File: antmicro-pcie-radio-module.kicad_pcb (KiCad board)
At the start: 4 copper layers, 80.2 x 22.2 mm, 54 parts, among them J1 U_FL-R-SMT_10_, J2 M.2-M+B-Pins, U1 UPD720202, U2 SST25VF512A, U3 CoralAccelerator, U4 NRF52840, U5 PE42423MLBA-Z, Y1 NX3225SA-24M

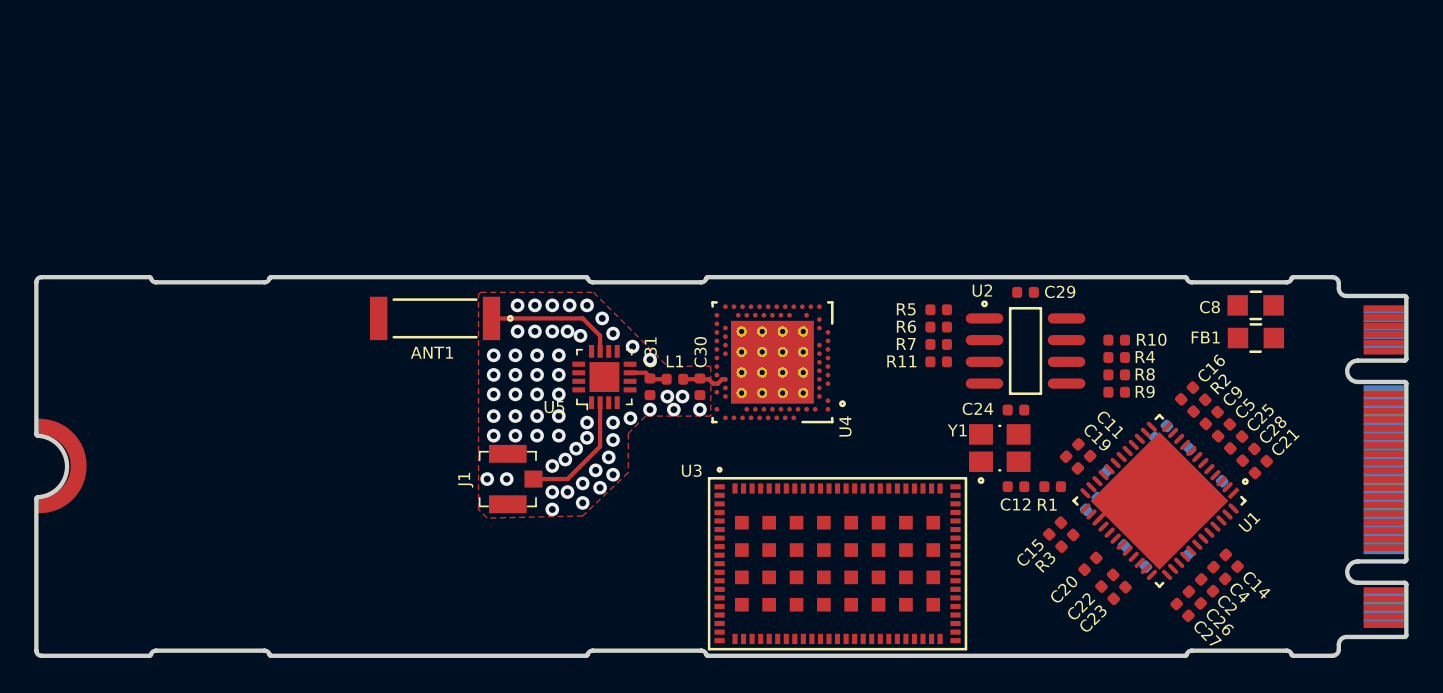
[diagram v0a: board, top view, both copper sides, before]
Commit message: Add initial component layout
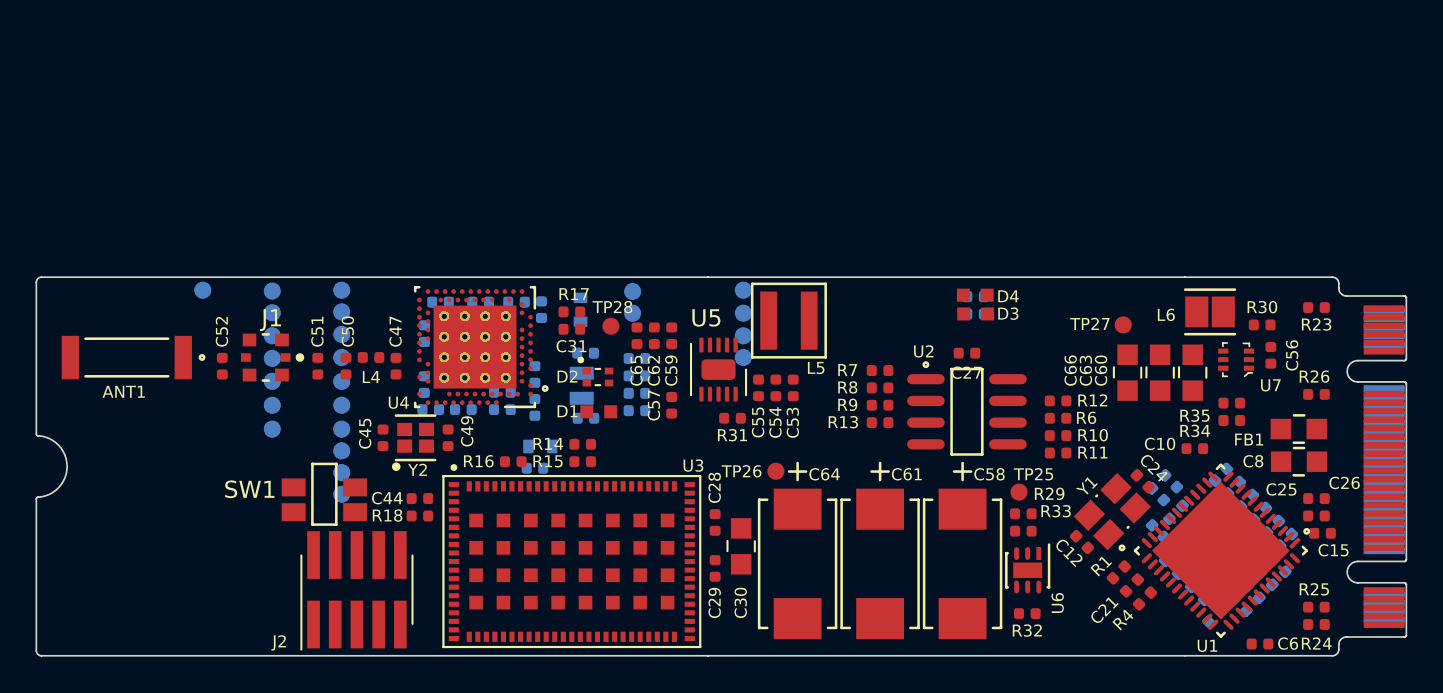
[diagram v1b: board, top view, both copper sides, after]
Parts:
- removed the C26 at (182.5, 110.2)
- removed the C27 at (181.8, 110.9)
- removed REF**: M.2 Stud, pcie-radio-module:M.2 Stud
- added C28: C_100n_0402, pcie-radio-module:0402-cap, F.Cu at (154.4, 105.8)
- added C29: C_100n_0402, pcie-radio-module:0402-cap, F.Cu at (154.4, 108.5)
- added C32: C_4u7_0402, pcie-radio-module:0402-cap, B.Cu at (142.8, 92.9)
- added C33: C_100n_0402, pcie-radio-module:0402-cap, B.Cu at (143.9, 97.1)
- added C34: C_100n_0402, pcie-radio-module:0402-cap, B.Cu at (139.7, 99.2)
- added C35: C_1u_0402, pcie-radio-module:0402-cap, B.Cu at (143.9, 99.1)
- added C36: C_100n_0402, pcie-radio-module:0402-cap, B.Cu at (140.7, 92.9)
- added C37: C_100p_0402, pcie-radio-module:0402-cap, B.Cu at (137.4, 97.7)
- added C38: C_820p_0402, pcie-radio-module:0402-cap, B.Cu at (137.4, 94.7)
- added C39: C_100n_0402, pcie-radio-module:0402-cap, B.Cu at (137.8, 99.2)
- added C40: C_4u7_0402, pcie-radio-module:0402-cap, B.Cu at (144.3, 93.3)
- added C41: C_100n_0402, pcie-radio-module:0402-cap, B.Cu at (138.4, 92.9)
- added C42: C_1u_0402, pcie-radio-module:0402-cap, B.Cu at (142.0, 99.2)
- added C43: C_47n_0402, pcie-radio-module:0402-cap, B.Cu at (142.0, 98.2)
- added C44: C_100n_0402, pcie-radio-module:0402-cap, F.Cu at (137.2, 104.4)
- added C45: C_8p_0402, pcie-radio-module:0402-cap, F.Cu at (135.0, 100.8)
- added C46: C_12p_0402, pcie-radio-module:0402-cap, B.Cu at (146.9, 99.7)
- added C47: C_0p8_0402, pcie-radio-module:0402-cap, F.Cu at (135.8, 96.6)
- added C48: C_12p_0402, pcie-radio-module:0402-cap, B.Cu at (146.9, 95.9)
- added C49: C_8p_0402, pcie-radio-module:0402-cap, F.Cu at (138.8, 100.8)
- added C50: C_0p5_0402, pcie-radio-module:0402-cap, F.Cu at (132.8, 96.6)
- added C51: RF_Capacitor, pcie-radio-module:0402-cap, F.Cu at (131.2, 96.6)
- added C52: C_1p2_0402, pcie-radio-module:0402-cap, F.Cu at (125.6, 96.6)
- added C53: C_10u_0402, pcie-radio-module:0402-cap, F.Cu at (159.0, 97.9)
- added C54: C_10u_0402, pcie-radio-module:0402-cap, F.Cu at (158.0, 97.9)
- added C55: C_10u_0402, pcie-radio-module:0402-cap, F.Cu at (157.0, 97.9)
- added C56: C_4u7_0402, pcie-radio-module:0402-cap, F.Cu at (186.9, 96.0)
- added C57: C_10n_0402, pcie-radio-module:0402-cap, F.Cu at (151.9, 98.9)
- added C58: C_330u_EEF-SX, pcie-radio-module:Panasonic_Electronic_Components-CD-0-0-MFG, F.Cu at (168.9, 108.2)
- added C59: C_10u_0402, pcie-radio-module:0402-cap, F.Cu at (151.9, 94.9)
- added C60: C_22u_0805_10V, pcie-radio-module:0805-cap, F.Cu at (182.4, 97.0)
- added C61: C_330u_EEF-SX, pcie-radio-module:Panasonic_Electronic_Components-CD-0-0-MFG, F.Cu at (164.1, 108.2)
- added C62: C_10u_0402, pcie-radio-module:0402-cap, F.Cu at (150.9, 94.9)
- added C63: C_22u_0805_10V, pcie-radio-module:0805-cap, F.Cu at (180.5, 97.0)
- added C64: C_330u_EEF-SX, pcie-radio-module:Panasonic_Electronic_Components-CD-0-0-MFG, F.Cu at (159.3, 108.2)
- added C65: C_10u_0402, pcie-radio-module:0402-cap, F.Cu at (149.9, 94.9)
- added C66: C_22u_0805_10V, pcie-radio-module:0805-cap, F.Cu at (178.6, 97.0)
- added D1: KP-1608CGCK, pcie-radio-module:LED0603, F.Cu at (147.6, 99.3)
- added D2: APHF1608LSEEQBDZGKC, pcie-radio-module:LED_APHF1608LSEEQBDZGKC, F.Cu at (147.6, 97.3)
- added D3: KP-1608CGCK, pcie-radio-module:LED0603, F.Cu at (169.6, 93.6)
- added D4: KP-1608CGCK, pcie-radio-module:LED0603, F.Cu at (169.7, 92.5)
- added J2: 2X05, pcie-radio-module:ARM_SWD, F.Cu at (133.5, 109.5)
- added L2: L_10u_80mA_0603, pcie-radio-module:0603-res, B.Cu at (146.6, 93.3)
- added L3: L_15n_0402, pcie-radio-module:0402-res, B.Cu at (143.9, 102.6)
- added L4: L_4n7_0402, pcie-radio-module:0402-res, F.Cu at (134.3, 96.1)
- added L5: XFL4020-102MEC, pcie-radio-module:Coilcraft-XFL4020-0-0-MFG, F.Cu at (158.7, 94.0)
- added L6: DFE201610E-1R0M=P2, pcie-radio-module:Murata-DFE201610C-0-0-IPC_B, F.Cu at (183.4, 93.5)
- added R14: R_4k3_0402, antmicro-footprints:0402-res, F.Cu at (146.7, 101.2)
- added R15: R_4k7_0402, pcie-radio-module:0402-res, F.Cu at (146.7, 102.2)
- added R16: R_4k3_0402, antmicro-footprints:0402-res, F.Cu at (142.6, 102.2)
- added R17: R_4R7_0402, antmicro-footprints:0402-res, F.Cu at (146.1, 93.5)
- added R18: R_10k_0402, pcie-radio-module:0402-res, F.Cu at (137.2, 105.4)
- added R19: R_330R_0402, antmicro-footprints:0402-res, B.Cu at (149.9, 99.3)
- added R20: R_2k2_0402, pcie-radio-module:0402-res, B.Cu at (149.9, 96.2)
- added R21: R_390R_0402, pcie-radio-module:0402-res, B.Cu at (149.9, 97.2)
- added R22: R_1k2_0402, pcie-radio-module:0402-res, B.Cu at (149.9, 98.2)
- added R23: R_0R_0402, antmicro-footprints:0402-res, F.Cu at (189.6, 93.2)
- added R24: R_0R_0402, antmicro-footprints:0402-res, F.Cu at (189.6, 111.8)
- added R25: R_0R_0402, antmicro-footprints:0402-res, F.Cu at (189.6, 110.7)
- added R26: R_0R_0402, antmicro-footprints:0402-res, F.Cu at (189.6, 98.3)
- added R27: R_330R_0402, antmicro-footprints:0402-res, B.Cu at (169.7, 93.6)
- added R28: R_330R_0402, antmicro-footprints:0402-res, B.Cu at (169.7, 92.6)
- added R29: R_10k_0402, pcie-radio-module:0402-res, F.Cu at (172.5, 105.3)
- added R3: R_10k_0402, pcie-radio-module:0402-res, B.Cu at (180.3, 104.1)
- added R30: R_0R_0402, antmicro-footprints:0402-res, F.Cu at (186.4, 94.2)
- added R31: R_0R_0402, antmicro-footprints:0402-res, F.Cu at (155.4, 99.7)
- added R32: R_0R_0402, antmicro-footprints:0402-res, F.Cu at (172.7, 111.1)
- added R33: R_21k_0402, pcie-radio-module:0402-res, F.Cu at (172.5, 106.3)
- added R34: R_75k_0402, pcie-radio-module:0402-res, F.Cu at (184.7, 99.8)
- added R35: R_100k_0402, pcie-radio-module:0402-res, F.Cu at (184.7, 98.8)
- added R5: R_10k_0402, pcie-radio-module:0402-res, B.Cu at (181.1, 103.4)
- added SW1: PTS840_GK_SMTR_LFS, pcie-radio-module:CK-PTS840_GK_SMTR_LFS-0, F.Cu at (131.6, 104.1)
- added TP1: TP_SMD1MM, antmicro-footprints:Testpoint_smd_1mm, B.Cu at (132.6, 101.5)
- added TP10: TP_SMD1MM, antmicro-footprints:Testpoint_smd_1mm, B.Cu at (128.5, 92.2)
- added TP11: TP_SMD1MM, antmicro-footprints:Testpoint_smd_1mm, B.Cu at (132.6, 92.2)
- added TP12: TP_SMD1MM, antmicro-footprints:Testpoint_smd_1mm, B.Cu at (132.6, 93.4)
- added TP13: TP_SMD1MM, antmicro-footprints:Testpoint_smd_1mm, B.Cu at (156.1, 93.6)
- added TP14: TP_SMD1MM, antmicro-footprints:Testpoint_smd_1mm, B.Cu at (132.6, 102.8)
- added TP15: TP_SMD1MM, antmicro-footprints:Testpoint_smd_1mm, B.Cu at (132.6, 104.1)
- added TP16: TP_SMD1MM, antmicro-footprints:Testpoint_smd_1mm, B.Cu at (132.6, 94.7)
- added TP17: TP_SMD1MM, antmicro-footprints:Testpoint_smd_1mm, B.Cu at (128.5, 94.8)
- added TP18: TP_SMD1MM, antmicro-footprints:Testpoint_smd_1mm, B.Cu at (128.5, 93.5)
- added TP19: TP_SMD1MM, antmicro-footprints:Testpoint_smd_1mm, B.Cu at (132.6, 96.1)
- added TP2: TP_SMD1MM, antmicro-footprints:Testpoint_smd_1mm, B.Cu at (156.1, 92.3)
- added TP20: TP_SMD1MM, antmicro-footprints:Testpoint_smd_1mm, B.Cu at (132.6, 97.5)
- added TP21: TP_SMD1MM, antmicro-footprints:Testpoint_smd_1mm, B.Cu at (132.6, 98.9)
- added TP22: TP_SMD1MM, antmicro-footprints:Testpoint_smd_1mm, B.Cu at (128.5, 97.5)
- added TP23: TP_SMD1MM, antmicro-footprints:Testpoint_smd_1mm, B.Cu at (128.5, 100.3)
- added TP24: TP_SMD1MM, antmicro-footprints:Testpoint_smd_1mm, B.Cu at (132.6, 100.3)
- added TP25: TP_SMD1MM, antmicro-footprints:Testpoint_smd_1mm, F.Cu at (172.2, 104.0)
- added TP26: TP_SMD1MM, antmicro-footprints:Testpoint_smd_1mm, F.Cu at (158.0, 102.7)
- added TP27: TP_SMD1MM, antmicro-footprints:Testpoint_smd_1mm, F.Cu at (178.3, 94.3)
- added TP28: TP_SMD1MM, antmicro-footprints:Testpoint_smd_1mm, F.Cu at (148.3, 94.4)
- added TP3: TP_SMD1MM, antmicro-footprints:Testpoint_smd_1mm, B.Cu at (128.5, 96.1)
- added TP4: TP_SMD1MM, antmicro-footprints:Testpoint_smd_1mm, B.Cu at (128.5, 98.9)
- added TP5: TP_SMD1MM, antmicro-footprints:Testpoint_smd_1mm, B.Cu at (156.1, 96.2)
- added TP6: TP_SMD1MM, antmicro-footprints:Testpoint_smd_1mm, B.Cu at (149.6, 93.6)
- added TP7: TP_SMD1MM, antmicro-footprints:Testpoint_smd_1mm, B.Cu at (156.1, 94.9)
- added TP8: TP_SMD1MM, antmicro-footprints:Testpoint_smd_1mm, B.Cu at (149.6, 92.3)
- added TP9: TP_SMD1MM, antmicro-footprints:Testpoint_smd_1mm, B.Cu at (124.5, 92.2)
- added U6: NCP380HMUAJAATBG, pcie-radio-module:ON_Semiconductor-517AB-04_2013-C-IPC_B, F.Cu at (172.7, 108.6)
- added U7: TLV62568PDRLT, pcie-radio-module:SOT-563, F.Cu at (184.9, 96.3)
- added Y2: ABM11W-101-32.0000MHZ-T3, pcie-radio-module:Abracon-ABM11W-0-0-0, F.Cu at (136.9, 100.8)
- added Y3: ABS06-32.768KHZ-9-1-T, pcie-radio-module:Abracon-ABS06-32.768KHZ-T-0, B.Cu at (146.6, 97.8)
- C10, C6: moved to F.Cu
- C11, C14, C16, C19, C2, C20, C22, C23, C4, C5, C9, R2: moved to B.Cu
- C30: value RF_Capacitor -> C_10u_0805; footprint pcie-radio-module:0402-cap -> pcie-radio-module:0805-cap
- C31: value RF_Capacitor -> C_4u7_0402
- J1: value U_FL-R-SMT_10_ -> MM8130-2600RA2; footprint pcie-radio-module:Coax_Conn_U.FL -> pcie-radio-module:Murata-MM8130-2600RA2-MFG
- L1: value RF_Inductor -> L_10u_250mA_0603; footprint pcie-radio-module:0402-res -> pcie-radio-module:0603-res; moved to B.Cu
- U5: value PE42423MLBA-Z -> TPS61232DRCR; footprint pcie-radio-module:VFQFN-16-1EP_3x3mm -> pcie-radio-module:VSON-10-1EP_3x3mm
- moved ANT1 18.2 mm to (120.0, 96.1)
- moved U4 17.4 mm to (140.4, 95.5)
- moved J1 15.8 mm to (128.1, 96.1), turned to 270 degrees
- moved C15 15.6 mm to (190.0, 106.4), turned to 0 degrees
- moved U3 15.5 mm to (146.1, 108.1)
- moved C6 13.7 mm to (186.3, 112.9), turned to 0 degrees
- moved C19 12.2 mm to (183.6, 111.3), turned to 45 degrees
- moved C18 11.5 mm to (187.8, 106.8), turned to 225 degrees
- moved C21 10.2 mm to (178.8, 109.5), turned to 225 degrees
- moved C11 9.97 mm to (185.5, 104.5), turned to 225 degrees
- moved C20 9.68 mm to (185.9, 109.9), turned to 135 degrees
- moved C30 9.64 mm to (156.0, 107.2)
- moved C5 9.62 mm to (183.4, 110.0)
- moved C23 9.49 mm to (187.5, 108.3), turned to 135 degrees
- moved C8 9.49 mm to (188.6, 102.2), turned to 0 degrees
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- renumbered C28 to C26, C29 to C27, J2 to J3, R8 to R10, R9 to R11, R10 to R12, R11 to R13, R3 to R4, R4 to R6, R5 to R7, R6 to R8, R7 to R9
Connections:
- net 1V0 renamed 1V05
- net Net-(U4-PadB5) renamed /nRF52840/DEC4_6
- C30 pad 1: Net-(C30-Pad1) -> 3V3_CORAL
- J1 pad 1: GND -> Net-(C50-Pad1)
- J1 pad 2: Net-(J1-Pad2) -> Net-(ANT1-Pad1)
- J3 pad 1: Net-(J2-Pad1) -> /M2-Pins/CFG3
- J3 pad 2: Net-(J2-Pad2) -> 3V3
- J3 pad 21: Net-(J2-Pad21) -> /M2-Pins/CFG0
- J3 pad 27: Net-(J2-Pad27) -> GND
- J3 pad 3: Net-(J2-Pad3) -> GND
- J3 pad 33: Net-(J2-Pad33) -> GND
- J3 pad 39: Net-(J2-Pad39) -> GND
- J3 pad 4: Net-(J2-Pad4) -> 3V3
- J3 pad 45: Net-(J2-Pad45) -> GND
- J3 pad 51: Net-(J2-Pad51) -> GND
- J3 pad 57: Net-(J2-Pad57) -> GND
- J3 pad 69: Net-(J2-Pad69) -> /M2-Pins/CFG1
- J3 pad 70: Net-(J2-Pad70) -> 3V3
- J3 pad 71: Net-(J2-Pad71) -> GND
- J3 pad 72: Net-(J2-Pad72) -> 3V3
- J3 pad 73: Net-(J2-Pad73) -> GND
- J3 pad 74: Net-(J2-Pad74) -> 3V3
- J3 pad 75: Net-(J2-Pad75) -> /M2-Pins/CFG2
- J3 pad 9: Net-(J2-Pad9) -> GND
- L1 pad 1: Net-(C30-Pad1) -> Net-(L1-Pad1)
- L1 pad 2: Net-(C31-Pad1) -> Net-(L1-Pad2)
- U1 pad 31: Net-(U1-Pad31) -> GND
- U1 pad 32: Net-(U1-Pad32) -> GND
- U1 pad 40: Aux_USB3_Rx_P -> GND
- U1 pad 41: Aux_USB3_Rx_N -> GND
- U1 pad 44: Aux_USB3_P -> CORAL_USB_P
- U1 pad 45: Aux_USB3_N -> CORAL_USB_N
- U3 pad 10: Net-(U3-Pad10) -> GND
- U3 pad 11: Net-(U3-Pad11) -> GND
- U3 pad 13: Net-(U3-Pad13) -> CORAL_USB_P
- U3 pad 14: Net-(U3-Pad14) -> CORAL_USB_N
- U3 pad 37: Net-(U3-Pad37) -> CORAL_PGOOD
- U3 pad 53: Net-(U3-Pad53) -> CORAL_PMIC_EN
- U3 pad 54: Net-(U3-Pad54) -> 3V3_CORAL
- U3 pad 56: VIN -> 3V3_CORAL
- U3 pad 57: VIN -> 3V3_CORAL
- U3 pad 58: VIN -> 3V3_CORAL
- U3 pad 59: VIN -> 3V3_CORAL
- U3 pad 60: VIN -> 3V3_CORAL
- U3 pad 61: VIN -> 3V3_CORAL
- U3 pad 62: VIN -> 3V3_CORAL
- U3 pad 63: VIN -> 3V3_CORAL
- U3 pad 64: VIN -> 3V3_CORAL
- U3 pad 65: VIN -> 3V3_CORAL
- U3 pad 66: VIN -> 3V3_CORAL
- U3 pad 67: VIN -> 3V3_CORAL
- U3 pad 7: Net-(U3-Pad7) -> GND
- U3 pad 8: Net-(U3-Pad8) -> GND
- U4 pad A22: Net-(U4-PadA22) -> /nRF52840/VDD
- U4 pad A23: Net-(U4-PadA23) -> /nRF52840/XC2
- U4 pad AA24: Net-(U4-PadAA24) -> /nRF52840/SWCLK
- U4 pad AC11: Net-(U4-PadAC11) -> CORAL_RST
- U4 pad AC13: Net-(U4-PadAC13) -> /nRF52840/~RESET
- U4 pad AC15: Net-(U4-PadAC15) -> CORAL_PMIC_EN
- U4 pad AC17: Net-(U4-PadAC17) -> CORAL_PGOOD
- U4 pad AC24: Net-(U4-PadAC24) -> /nRF52840/SWDIO
- U4 pad AD14: Net-(U4-PadAD14) -> /nRF52840/VDD
- U4 pad AD2: Net-(U4-PadAD2) -> /nRF52840/VDD
- U4 pad AD23: Net-(U4-PadAD23) -> /nRF52840/VDD
- U4 pad AD4: Net-(U4-PadAD4) -> Radio_USB_N
- U4 pad AD6: Net-(U4-PadAD6) -> Radio_USB_P
- U4 pad B1: Net-(U4-PadB1) -> /nRF52840/VDD
- U4 pad B24: Net-(U4-PadB24) -> /nRF52840/XC1
- U4 pad B3: Net-(U4-PadB3) -> Net-(L1-Pad1)
- U4 pad D2: Net-(U4-PadD2) -> /nRF52840/XL1
- U4 pad F2: Net-(U4-PadF2) -> /nRF52840/XL2
- U4 pad H23: Net-(C30-Pad1) -> Net-(C47-Pad1)
- U4 pad L1: Net-(U4-PadL1) -> /nRF52840/LED1
- U4 pad N1: Net-(U4-PadN1) -> /nRF52840/LED2_R
- U4 pad R1: Net-(U4-PadR1) -> /nRF52840/LED2_G
- U4 pad U1: Net-(U4-PadU1) -> /nRF52840/LED2_B
- U4 pad W1: Net-(U4-PadW1) -> /nRF52840/VDD
- U4 pad Y2: Net-(U4-PadY2) -> Net-(C31-Pad1)
- U5 pad 1: GND -> Net-(L5-Pad2)
- U5 pad 10: GND -> 3V3
- U5 pad 11: Net-(ANT1-Pad1) -> GND
- U5 pad 2: Net-(J1-Pad2) -> Net-(L5-Pad2)
- U5 pad 3: GND -> 5V_RADIO
- U5 pad 4: GND -> 5V_RADIO
- U5 pad 5: GND -> /powerSupply/3V3_PG
- U5 pad 6: GND -> Net-(C57-Pad1)
- U5 pad 7: Net-(C31-Pad1) -> 5V_RADIO
- U5 pad 8: GND -> Net-(U5-Pad8)
- U5 pad 9: GND -> Net-(R31-Pad1)
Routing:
- net Net-(ANT1-Pad1): track 7.66 -> 0.00 mm
- net Net-(J1-Pad2): track 7.10 -> 0.00 mm
- net GND: track 4.10 -> 0.00 mm, vias 58 -> 0
- net Net-(C30-Pad1): track 2.65 -> 0.00 mm
- net Net-(C31-Pad1): track 2.30 -> 0.00 mm
- removed copper zone on F.Cu, net GND
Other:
- board size 80.2 x 22.2 mm -> 80.2 x 22.1 mm

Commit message: Layout: add signal traces
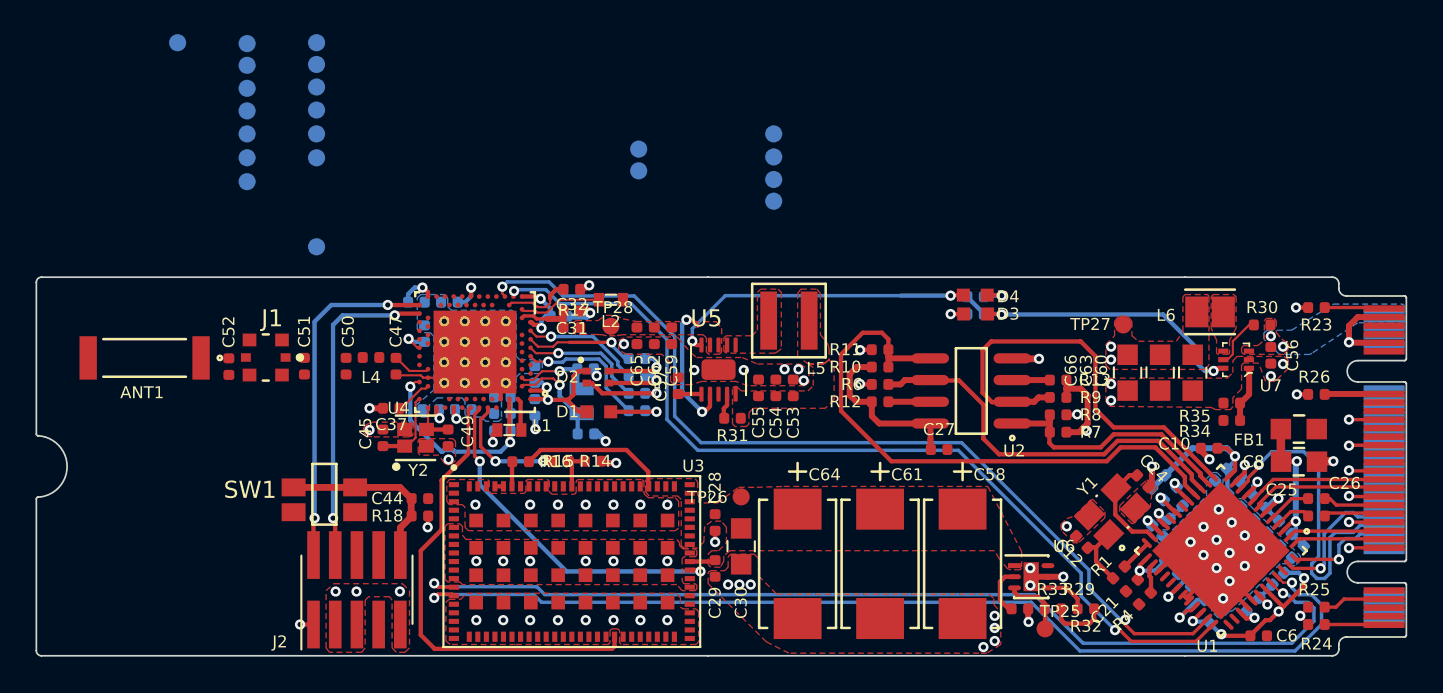
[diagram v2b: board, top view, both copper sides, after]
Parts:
- removed TP1, TP14, TP24: TP_SMD1MM, antmicro-footprints:Testpoint_smd_1mm
- C15: moved to B.Cu
- C32, C37, L1, L2: moved to F.Cu
- moved TP11 14.6 mm to (131.1, 77.7)
- moved TP15 14.6 mm to (131.1, 89.6)
- moved TP16 14.6 mm to (131.1, 80.3)
- moved TP17 14.6 mm to (127.1, 80.3)
- moved TP20 14.6 mm to (131.1, 83.0)
- moved TP22 14.6 mm to (127.1, 83.0)
- moved TP23 14.6 mm to (127.1, 85.8)
- moved TP9 14.6 mm to (123.0, 77.7)
- moved TP10 14.6 mm to (127.1, 77.7)
- moved TP12 14.6 mm to (131.1, 78.9)
- moved TP18 14.6 mm to (127.1, 79.0)
- moved TP19 14.6 mm to (131.1, 81.6)
- moved TP21 14.6 mm to (131.1, 84.4)
- moved TP3 14.6 mm to (127.1, 81.7)
- moved TP4 14.6 mm to (127.1, 84.4)
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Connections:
- U4 pad A10: Net-(TP14-Pad1) -> CORAL_RST
- U4 pad A12: Net-(TP1-Pad1) -> CORAL_PMIC_EN
- U4 pad A14: Net-(TP24-Pad1) -> CORAL_PGOOD
- U4 pad A16: Net-(TP23-Pad1) -> Net-(U4-PadA16)
- U4 pad A20: Net-(TP21-Pad1) -> Net-(U4-PadA20)
- U4 pad A8: Net-(TP15-Pad1) -> Net-(U4-PadA8)
- U4 pad AC11: CORAL_RST -> Net-(U4-PadAC11)
- U4 pad AC15: CORAL_PMIC_EN -> Net-(U4-PadAC15)
- U4 pad AC17: CORAL_PGOOD -> Net-(U4-PadAC17)
- U4 pad AC9: Net-(TP7-Pad1) -> Net-(U4-PadAC9)
- U4 pad AD10: Net-(TP8-Pad1) -> Net-(U4-PadAD10)
- U4 pad AD12: Net-(TP9-Pad1) -> Net-(U4-PadAD12)
- U4 pad AD16: Net-(TP10-Pad1) -> Net-(U4-PadAD16)
- U4 pad AD18: Net-(TP11-Pad1) -> Net-(U4-PadAD18)
- U4 pad AD20: Net-(TP12-Pad1) -> Net-(U4-PadAD20)
- U4 pad AD22: Net-(TP16-Pad1) -> Net-(U4-PadAD22)
- U4 pad AD8: Net-(TP6-Pad1) -> Net-(U4-PadAD8)
- U4 pad B19: Net-(TP22-Pad1) -> Net-(U4-PadB19)
- U4 pad G1: Net-(TP13-Pad1) -> Net-(U4-PadG1)
- U4 pad J1: Net-(TP2-Pad1) -> Net-(U4-PadJ1)
- U4 pad J24: Net-(TP4-Pad1) -> Net-(U4-PadJ24)
- U4 pad L24: Net-(TP3-Pad1) -> Net-(U4-PadL24)
- U4 pad P23: Net-(TP20-Pad1) -> Net-(U4-PadP23)
- U4 pad T2: Net-(TP5-Pad1) -> Net-(U4-PadT2)
- U4 pad U24: Net-(TP19-Pad1) -> Net-(U4-PadU24)
- U4 pad W24: Net-(TP18-Pad1) -> Net-(U4-PadW24)
- U4 pad Y23: Net-(TP17-Pad1) -> Net-(U4-PadY23)
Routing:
- net CORAL_USB_N: track 0.00 -> 60.2 mm, vias 0 -> 2
- net CORAL_USB_P: track 0.00 -> 59.0 mm, vias 0 -> 2
- net Radio_USB_P: track 0.00 -> 54.4 mm, vias 0 -> 2
- net Radio_USB_N: track 0.00 -> 53.8 mm, vias 0 -> 2
- net 3V3: track 0.00 -> 45.6 mm, vias 0 -> 9
- net GND: track 0.00 -> 44.7 mm, vias 0 -> 87
- net Net-(R10-Pad2): track 0.00 -> 34.9 mm
- net CORAL_PGOOD: track 0.00 -> 27.4 mm
- net Net-(R9-Pad2): track 0.00 -> 25.5 mm
- net Net-(R6-Pad1): track 0.00 -> 23.1 mm
- net CORAL_PMIC_EN: track 0.00 -> 20.4 mm, vias 0 -> 2
- net /nRF52840/SWDIO: track 0.00 -> 20.2 mm, vias 0 -> 2
- net ~PECREQ: track 0.00 -> 19.3 mm, vias 0 -> 1
- net /nRF52840/SWCLK: track 0.00 -> 18.8 mm, vias 0 -> 2
- net 1V05: track 0.00 -> 18.7 mm, vias 0 -> 9
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- added copper zone on F.Cu, net 1V05
- added copper zone on B.Cu, net 3V3
- added copper zone on F.Cu, net 3V3
- added copper zone on F.Cu, net 3V3_CORAL
- added copper zone on F.Cu, net 5V_RADIO
- added copper zone on B.Cu, net GND
- added copper zone on F.Cu, net GND
- added copper zone on In1.Cu, net GND
- added copper zone on In2.Cu, net GND
- added copper zone on F.Cu, net Net-(L5-Pad2)
- added copper zone on F.Cu, net Net-(L6-Pad1)
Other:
- net class Diff_90 added: clearance 0.127, trace_width 0.28, via_dia 0.8, via_drill 0.4
- rule trace_min: 0.2 -> 0.12

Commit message: Layout: add power planes
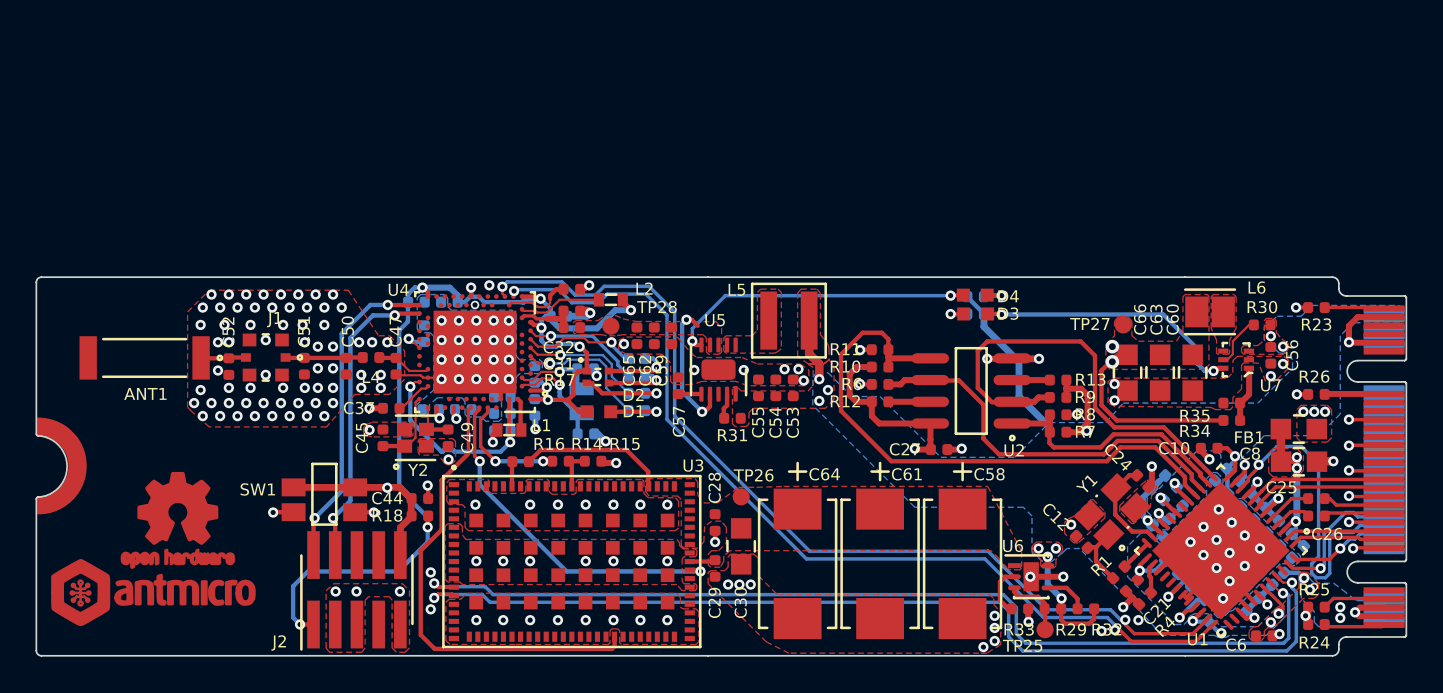
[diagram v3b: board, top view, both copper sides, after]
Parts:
- removed TP10, TP11, TP12, TP13, TP15, TP16, TP17, TP18, TP19, TP2, TP20, TP21, TP22, TP23, TP3, TP4, TP5, TP6, TP7, TP8, TP9: TP_SMD1MM, antmicro-footprints:Testpoint_smd_1mm
- added G***: LOGO, antmicro-footprints:antmicro-logo_scaled_12mm, F.Cu at (121.5, 109.9)
- added REF**: OSHW-Logo2_7.3x6mm_Copper_Mask, antmicro-footprints:OSHW-Logo2_7.3x6mm_Copper_Mask, F.Cu at (123.0, 105.7)
- added REF**: M.2 Stud, pcie-radio-module:M.2 Stud, F.Cu at (115.3, 102.4)
- moved C6 0.33 mm to (186.6, 112.4)
- moved TP25 0.05 mm to (173.7, 112.0)
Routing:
- net 1V05: track 18.7 -> 87.4 mm
- net /nRF52840/VDD: track 17.9 -> 77.5 mm, vias 8 -> 10
- net /nRF52840/~RESET: track 10.7 -> 29.9 mm, vias 0 -> 2
- net Net-(C13-Pad1): track 12.2 -> 24.7 mm, vias 3 -> 4
- net GND: track 44.7 -> 57.2 mm, vias 87 -> 183
- net 3V3: track 45.6 -> 53.4 mm, vias 9 -> 24
- net Net-(C50-Pad1): track 0.00 -> 4.62 mm
- net Net-(ANT1-Pad1): track 0.00 -> 2.67 mm
- net /nRF52840/SWDIO: track 20.2 -> 18.9 mm
- net CORAL_USB_N: track 60.2 -> 59.2 mm
- net CORAL_USB_P: track 59.0 -> 57.9 mm
- net /nRF52840/SWCLK: track 18.8 -> 17.8 mm
- net Net-(C47-Pad1): track 2.21 -> 3.10 mm
- net Radio_USB_N: track 53.8 -> 54.5 mm
- net Radio_USB_P: track 54.4 -> 55.1 mm
- added copper zone on F.Cu, net Net-(C13-Pad1)
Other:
- net class Default: clearance 0.127 -> 0.1
- rule trace_clearance: 0.127 -> 0.1

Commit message: Resolve DRC
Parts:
- removed G***: LOGO, antmicro-footprints:antmicro-logo_scaled_12mm
- removed REF**: OSHW-Logo2_7.3x6mm_Copper_Mask, antmicro-footprints:OSHW-Logo2_7.3x6mm_Copper_Mask
- removed REF**: M.2 Stud, pcie-radio-module:M.2 Stud
- added MP1: PCB_Mount_Hole_M2, pcie-radio-module:M.2-Stud, F.Cu at (115.3, 102.4)
- added N1: antmicro_logo, pcie-radio-module:antmicro-logo_scaled_12mm, F.Cu at (121.8, 109.7)
- added N2: oshw_logo, pcie-radio-module:OSHW-Logo2_7.3x6mm_Copper_Mask, F.Cu at (123.1, 105.7)
- J3: footprint pcie-radio-module:M.2 M+B Keys -> pcie-radio-module:M.2-M+B-Keys
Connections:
- U3 pad 50: Net-(U3-Pad49) -> Net-(U3-Pad50)
- U3 pad 52: Net-(U3-Pad49) -> Net-(U3-Pad52)
- U3 pad 84: Net-(U3-Pad49) -> Net-(U3-Pad84)
- U3 pad 85: Net-(U3-Pad49) -> Net-(U3-Pad85)
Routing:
- net CORAL_USB_P: track 57.9 -> 59.2 mm
- net /nRF52840/VDD: track 77.5 -> 78.5 mm
- net Net-(R7-Pad2): track 14.7 -> 13.9 mm
- net Net-(R6-Pad1): track 23.1 -> 22.4 mm
- net GND: track 57.2 -> 56.6 mm
- net Radio_USB_N: track 54.5 -> 55.1 mm
